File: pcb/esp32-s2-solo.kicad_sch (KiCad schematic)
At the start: 4 parts, among them U1 ESP32-S2-SOLO

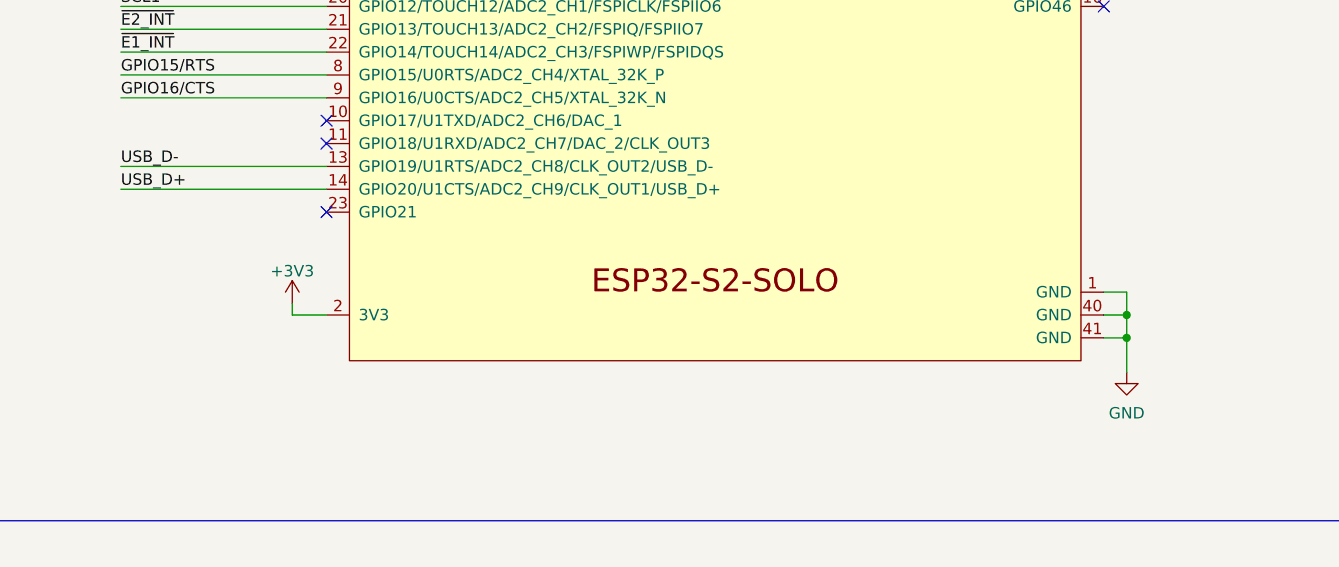
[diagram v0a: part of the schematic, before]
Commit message: fix ERC issues
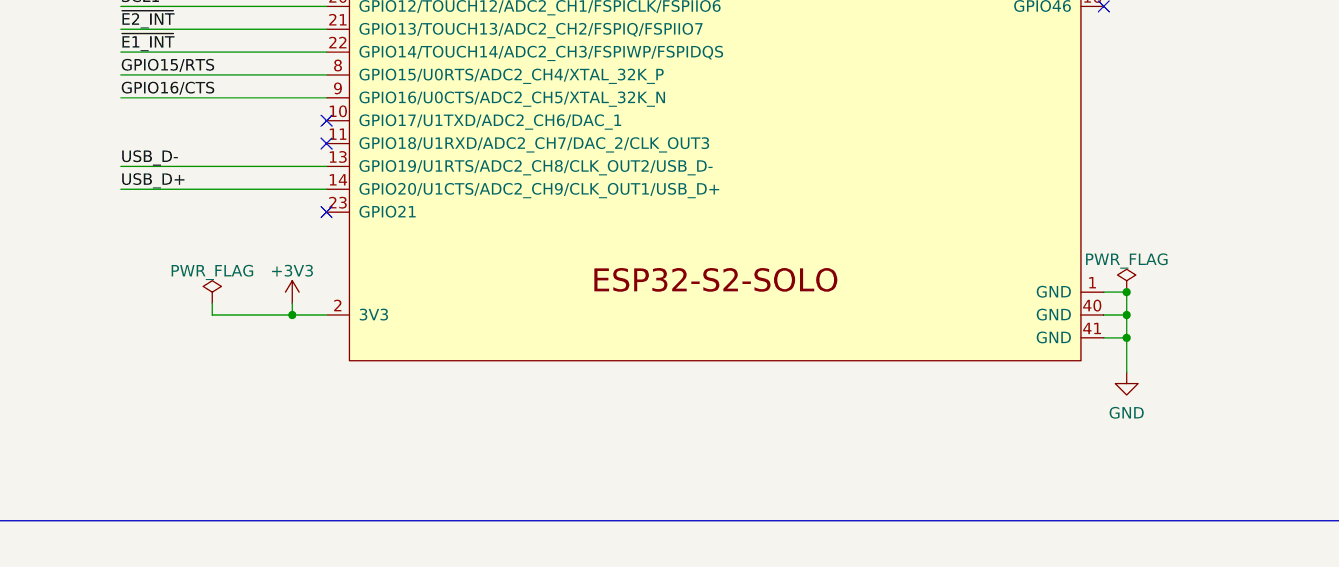
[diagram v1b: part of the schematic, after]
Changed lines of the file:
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@@
   (junction (at 250.19 115.57) (diameter 0) (color 0 0 0 0)
   )
+  (junction (at 157.48 115.57) (diameter 0) (color 0 0 0 0)
+  )
   (junction (at 68.58 172.72) (diameter 0) (color 0 0 0 0)
   )
@@
   )
   (junction (at 77.47 172.72) (diameter 0) (color 0 0 0 0)
+  )
+  (junction (at 250.19 113.03) (diameter 0) (color 0 0 0 0)
   )
   (no_connect (at 161.29 96.52))
@@
   (no_connect (at 247.65 57.15))
   (no_connect (at 247.65 54.61))
+  (wire (pts (xy 148.59 115.57) (xy 148.59 114.3))
+    (stroke (width 0) (type default) (color 0 0 0 0))
+  )
   (wire (pts (xy 161.29 86.36) (xy 138.43 86.36))
     (stroke (width 0) (type default) (color 0 0 0 0))
@@
   )
   (wire (pts (xy 29.21 175.26) (xy 29.21 180.34))
+    (stroke (width 0) (type default) (color 0 0 0 0))
+  )
+  (wire (pts (xy 157.48 115.57) (xy 148.59 115.57))
     (stroke (width 0) (type default) (color 0 0 0 0))
   )
@@
     )
     (property "Datasheet" "" (id 3) (at 74.93 162.56 0)
+      (effects (font (size 1.27 1.27)) hide)
+    )
+    (pin "1")
+  )
+  (symbol (lib_id "power:PWR_FLAG") (at 148.59 114.3 0) (unit 1)
+    (in_bom yes) (on_board yes) (fields_autoplaced)
+    (property "Reference" "#FLG0101" (id 0) (at 148.59 112.395 0)
+      (effects (font (size 1.27 1.27)) hide)
+    )
+    (property "Value" "PWR_FLAG" (id 1) (at 148.59 110.6955 0))
+    (property "Footprint" "" (id 2) (at 148.59 114.3 0)
+      (effects (font (size 1.27 1.27)) hide)
+    )
+    (property "Datasheet" "~" (id 3) (at 148.59 114.3 0)
       (effects (font (size 1.27 1.27)) hide)
     )
@@
       (effects (font (size 1.27 1.27)) hide)
     )
+    (pin "1")
+  )
+  (symbol (lib_id "power:PWR_FLAG") (at 250.19 113.03 0) (unit 1)
+    (in_bom yes) (on_board yes) (fields_autoplaced)
+    (property "Reference" "#FLG0102" (id 0) (at 250.19 111.125 0)
+      (effects (font (size 1.27 1.27)) hide)
+    )
+    (property "Value" "PWR_FLAG" (id 1) (at 250.19 109.4255 0))
+    (property "Footprint" "" (id 2) (at 250.19 113.03 0)
+      (effects (font (size 1.27 1.27)) hide)
+    )
+    (property "Datasheet" "~" (id 3) (at 250.19 113.03 0)
+      (effects (font (size 1.27 1.27)) hide)
+    )

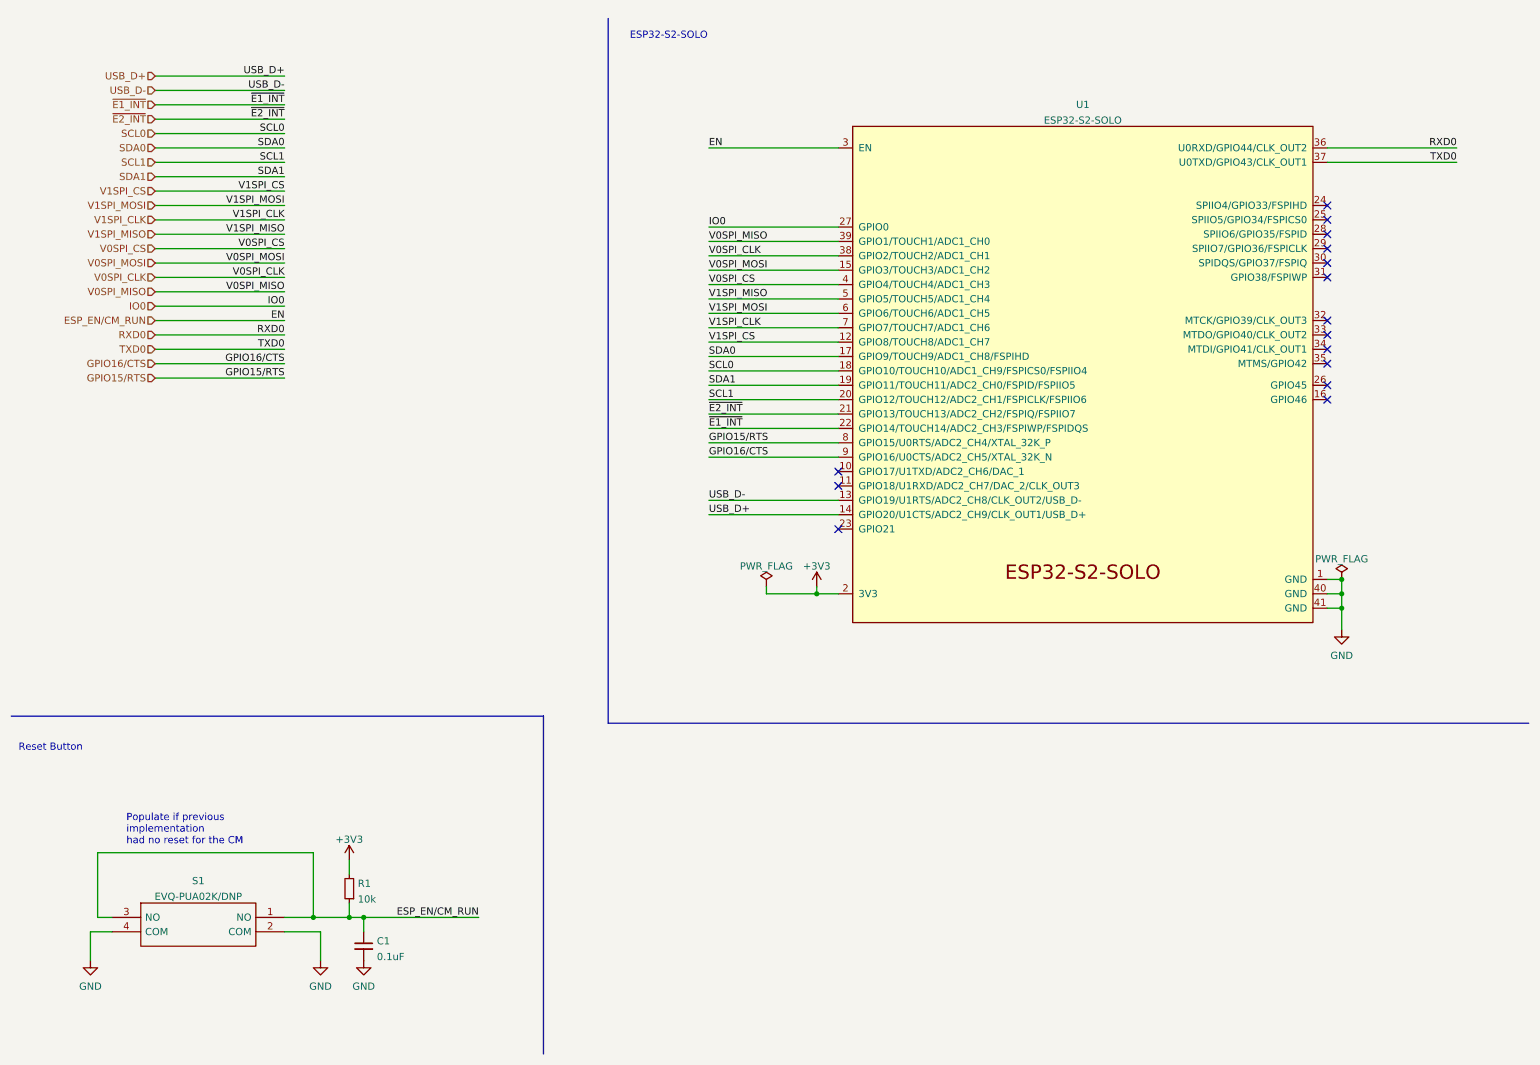
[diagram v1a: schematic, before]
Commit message: Refactored PCB Layer to have one dedicated GND Layer + rerouted traces + removed debug connector and added IO0 to the SO-DIMM connector + added decoupling caps and delay circuit for ESP32 module
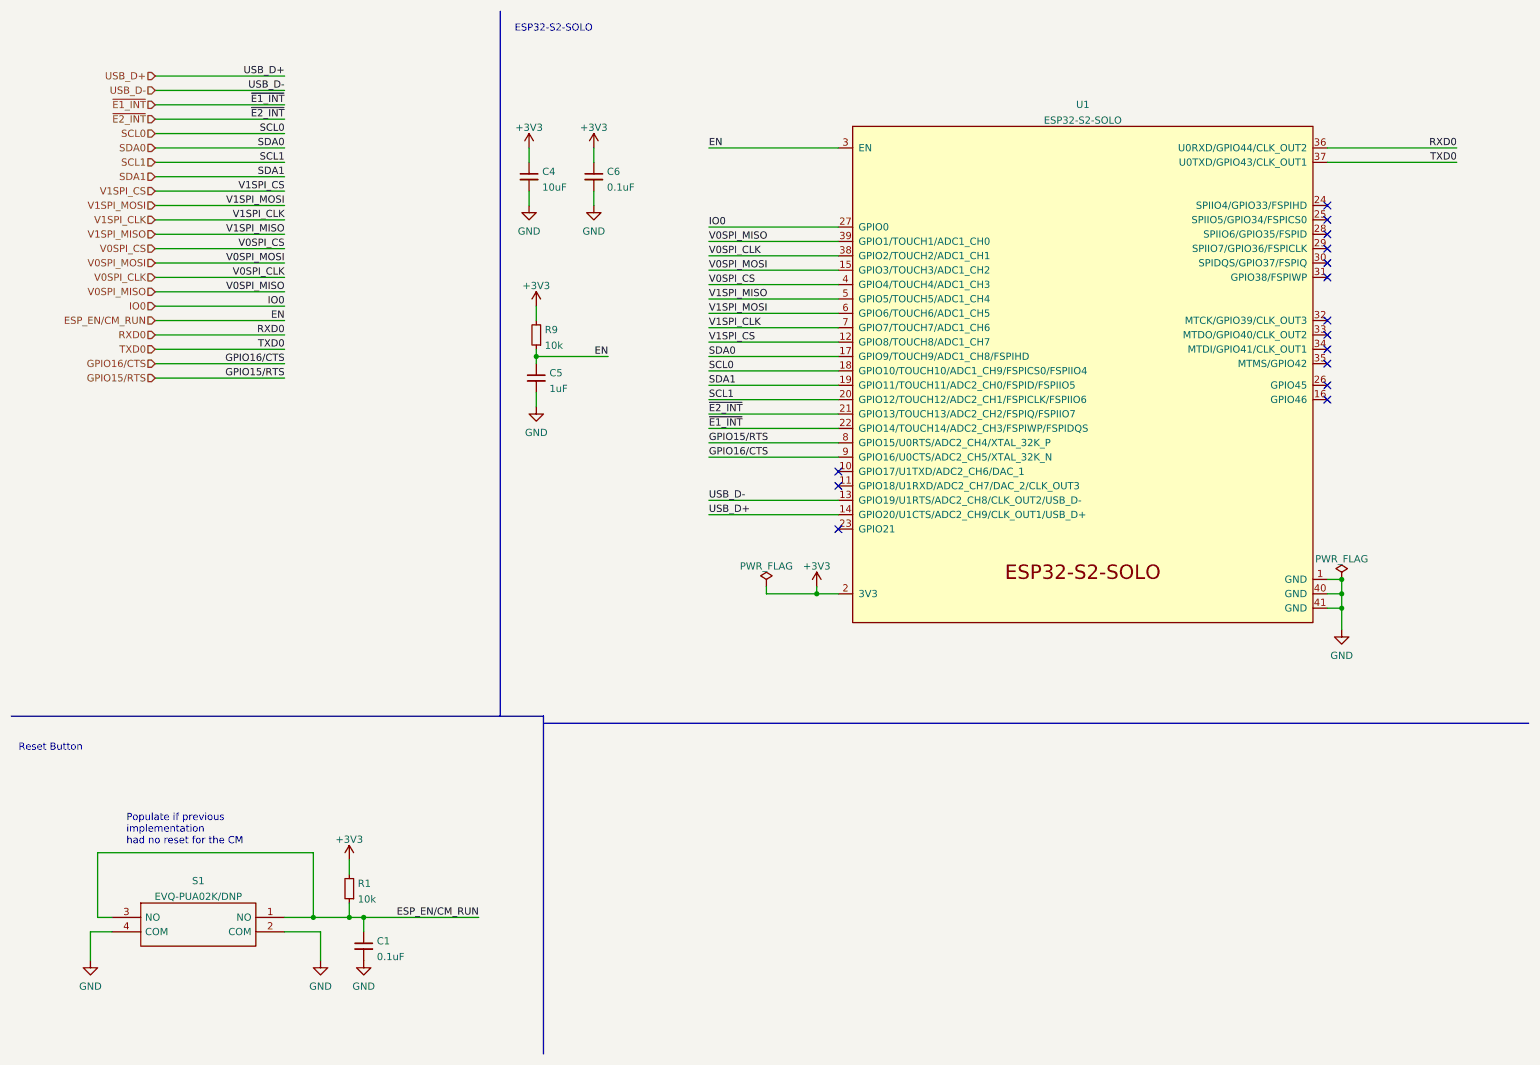
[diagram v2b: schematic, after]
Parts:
- added C4: 10uF, Capacitor_SMD:C_0603_1608Metric, symbol Device:C_Small
- added C5: 1uF, Capacitor_SMD:C_0603_1608Metric, symbol Device:C_Small
- added C6: 0.1uF, Capacitor_SMD:C_0603_1608Metric, symbol Device:C_Small
- added R9: 10k, Resistor_SMD:R_0603_1608Metric, symbol Device:R_Small
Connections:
- net +3V3: now also C4.1, C6.1, R9.2
- net ESP_EN/CM_RUN: now also C5.1, R9.1
- net GND: now also C4.2, C5.2, C6.2
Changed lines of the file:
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@@
   (junction (at 250.19 113.03) (diameter 0) (color 0 0 0 0)
+  )
+  (junction (at 107.95 73.66) (diameter 0) (color 0 0 0 0)
   )
   (no_connect (at 161.29 96.52))
@@
     (stroke (width 0) (type default) (color 0 0 0 0))
   )
-  (polyline (pts (xy 120.65 13.97) (xy 120.65 138.43))
+  (polyline (pts (xy 101.6 12.7) (xy 101.6 137.16))
     (stroke (width 0) (type default) (color 0 0 0 0))
   )
@@
     (stroke (width 0) (type default) (color 0 0 0 0))
   )
+  (wire (pts (xy 106.68 36.83) (xy 106.68 39.37))
+    (stroke (width 0) (type default) (color 0 0 0 0))
+  )
   (wire (pts (xy 161.29 115.57) (xy 157.48 115.57))
     (stroke (width 0) (type default) (color 0 0 0 0))
@@
     (stroke (width 0) (type default) (color 0 0 0 0))
   )
+  (wire (pts (xy 107.95 72.39) (xy 107.95 73.66))
+    (stroke (width 0) (type default) (color 0 0 0 0))
+  )
+  (wire (pts (xy 107.95 64.77) (xy 107.95 67.31))
+    (stroke (width 0) (type default) (color 0 0 0 0))
+  )
   (wire (pts (xy 40.64 54.61) (xy 63.5 54.61))
     (stroke (width 0) (type default) (color 0 0 0 0))
   )
-  (polyline (pts (xy 283.21 138.43) (xy 120.65 138.43))
+  (polyline (pts (xy 283.21 138.43) (xy 109.22 138.43))
+    (stroke (width 0) (type default) (color 0 0 0 0))
+  )
+  (wire (pts (xy 107.95 73.66) (xy 120.65 73.66))
+    (stroke (width 0) (type default) (color 0 0 0 0))
+  )
+  (wire (pts (xy 107.95 80.01) (xy 107.95 82.55))
     (stroke (width 0) (type default) (color 0 0 0 0))
   )
@@
     (stroke (width 0) (type default) (color 0 0 0 0))
   )
+  (wire (pts (xy 107.95 73.66) (xy 107.95 74.93))
+    (stroke (width 0) (type default) (color 0 0 0 0))
+  )
+  (wire (pts (xy 118.11 44.45) (xy 118.11 46.99))
+    (stroke (width 0) (type default) (color 0 0 0 0))
+  )
   (wire (pts (xy 157.48 115.57) (xy 157.48 114.3))
     (stroke (width 0) (type default) (color 0 0 0 0))
@@
     (stroke (width 0) (type default) (color 0 0 0 0))
   )
+  (wire (pts (xy 118.11 36.83) (xy 118.11 39.37))
+    (stroke (width 0) (type default) (color 0 0 0 0))
+  )
   (wire (pts (xy 29.21 175.26) (xy 29.21 180.34))
     (stroke (width 0) (type default) (color 0 0 0 0))
@@
     (stroke (width 0) (type default) (color 0 0 0 0))
   )
+  (wire (pts (xy 106.68 44.45) (xy 106.68 46.99))
+    (stroke (width 0) (type default) (color 0 0 0 0))
+  )
   (wire (pts (xy 138.43 36.83) (xy 161.29 36.83))
     (stroke (width 0) (type default) (color 0 0 0 0))
@@
     (stroke (width 0) (type default) (color 0 0 0 0))
   )
-  (text "ESP32-S2-SOLO" (at 124.46 17.78 0)
+  (text "ESP32-S2-SOLO" (at 104.14 16.51 0)
     (effects (font (size 1.27 1.27)) (justify left bottom))
   )
@@
     (effects (font (size 1.27 1.27)) (justify right bottom))
   )
+  (label "EN" (at 120.65 73.66 180)
+    (effects (font (size 1.27 1.27)) (justify right bottom))
+  )
   (label "SCL0" (at 138.43 76.2 0)
     (effects (font (size 1.27 1.27)) (justify left bottom))
@@
   (hierarchical_label "SCL1" (shape input) (at 40.64 39.37 180)
     (effects (font (size 1.27 1.27)) (justify right))
+  )
+  (symbol (lib_id "Device:C_Small") (at 107.95 77.47 0) (unit 1)
+    (in_bom yes) (on_board yes) (fields_autoplaced)
+    (property "Reference" "C5" (id 0) (at 110.2741 76.5678 0)
+      (effects (font (size 1.27 1.27)) (justify left))
+    )
+    (property "Value" "1uF" (id 1) (at 110.2741 79.3429 0)
+      (effects (font (size 1.27 1.27)) (justify left))
+    )
+    (property "Footprint" "Capacitor_SMD:C_0603_1608Metric" (id 2) (at 107.95 77.47 0)
+      (effects (font (size 1.27 1.27)) hide)
+    )
+    (property "Datasheet" "~" (id 3) (at 107.95 77.47 0)
+      (effects (font (size 1.27 1.27)) hide)
+    )
+    (pin "1")
+    (pin "2")
   )
   (symbol (lib_id "power:GND") (at 250.19 121.92 0) (unit 1)
@@
     )
     (property "Datasheet" "" (id 3) (at 250.19 121.92 0)
+      (effects (font (size 1.27 1.27)) hide)
+    )
+    (pin "1")
+  )
+  (symbol (lib_id "power:GND") (at 106.68 46.99 0) (unit 1)
+    (in_bom yes) (on_board yes) (fields_autoplaced)
+    (property "Reference" "#PWR0137" (id 0) (at 106.68 53.34 0)
+      (effects (font (size 1.27 1.27)) hide)
+    )
+    (property "Value" "GND" (id 1) (at 106.68 51.5525 0))
+    (property "Footprint" "" (id 2) (at 106.68 46.99 0)
+      (effects (font (size 1.27 1.27)) hide)
+    )
+    (property "Datasheet" "" (id 3) (at 106.68 46.99 0)
       (effects (font (size 1.27 1.27)) hide)
     )
@@
     (pin "1")
   )
+  (symbol (lib_id "Device:C_Small") (at 106.68 41.91 0) (unit 1)
+    (in_bom yes) (on_board yes) (fields_autoplaced)
+    (property "Reference" "C4" (id 0) (at 109.0041 41.0078 0)
+      (effects (font (size 1.27 1.27)) (justify left))
+    )
+    (property "Value" "10uF" (id 1) (at 109.0041 43.7829 0)
+      (effects (font (size 1.27 1.27)) (justify left))
+    )
+    (property "Footprint" "Capacitor_SMD:C_0603_1608Metric" (id 2) (at 106.68 41.91 0)
+      (effects (font (size 1.27 1.27)) hide)
+    )
+    (property "Datasheet" "~" (id 3) (at 106.68 41.91 0)
+      (effects (font (size 1.27 1.27)) hide)
+    )
+    (pin "1")
+    (pin "2")
+  )
+  (symbol (lib_id "power:+3V3") (at 106.68 36.83 0) (unit 1)
+    (in_bom yes) (on_board yes) (fields_autoplaced)
+    (property "Reference" "#PWR0136" (id 0) (at 106.68 40.64 0)
+      (effects (font (size 1.27 1.27)) hide)
+    )
+    (property "Value" "+3V3" (id 1) (at 106.68 33.2255 0))
+    (property "Footprint" "" (id 2) (at 106.68 36.83 0)
+      (effects (font (size 1.27 1.27)) hide)
+    )
+    (property "Datasheet" "" (id 3) (at 106.68 36.83 0)
+      (effects (font (size 1.27 1.27)) hide)
+    )
+    (pin "1")
+  )
   (symbol (lib_id "power:GND") (at 29.21 180.34 0) (unit 1)
     (in_bom yes) (on_board yes) (fields_autoplaced)
@@
     (pin "1")
   )
+  (symbol (lib_id "power:GND") (at 118.11 46.99 0) (unit 1)
+    (in_bom yes) (on_board yes) (fields_autoplaced)
+    (property "Reference" "#PWR0135" (id 0) (at 118.11 53.34 0)
+      (effects (font (size 1.27 1.27)) hide)
+    )
+    (property "Value" "GND" (id 1) (at 118.11 51.5525 0))
+    (property "Footprint" "" (id 2) (at 118.11 46.99 0)
+      (effects (font (size 1.27 1.27)) hide)
+    )
+    (property "Datasheet" "" (id 3) (at 118.11 46.99 0)
+      (effects (font (size 1.27 1.27)) hide)
+    )
+    (pin "1")
+  )
+  (symbol (lib_id "Device:R_Small") (at 107.95 69.85 180) (unit 1)
+    (in_bom yes) (on_board yes) (fields_autoplaced)
+    (property "Reference" "R9" (id 0) (at 109.4486 68.9415 0)
+      (effects (font (size 1.27 1.27)) (justify right))
+    )
+    (property "Value" "10k" (id 1) (at 109.4486 71.7166 0)
+      (effects (font (size 1.27 1.27)) (justify right))
+    )
+    (property "Footprint" "Resistor_SMD:R_0603_1608Metric" (id 2) (at 107.95 69.85 0)
+      (effects (font (size 1.27 1.27)) hide)
+    )
+    (property "Datasheet" "~" (id 3) (at 107.95 69.85 0)
+      (effects (font (size 1.27 1.27)) hide)
+    )
+    (pin "1")
+    (pin "2")
+  )
   (symbol (lib_id "Device:C_Small") (at 77.47 177.8 0) (unit 1)
     (in_bom yes) (on_board yes) (fields_autoplaced)
@@
     (pin "2")
   )
+  (symbol (lib_id "Device:C_Small") (at 118.11 41.91 0) (unit 1)
+    (in_bom yes) (on_board yes) (fields_autoplaced)
+    (property "Reference" "C6" (id 0) (at 120.4341 41.0078 0)
+      (effects (font (size 1.27 1.27)) (justify left))
+    )
+    (property "Value" "0.1uF" (id 1) (at 120.4341 43.7829 0)
+      (effects (font (size 1.27 1.27)) (justify left))
+    )
+    (property "Footprint" "Capacitor_SMD:C_0603_1608Metric" (id 2) (at 118.11 41.91 0)
+      (effects (font (size 1.27 1.27)) hide)
+    )
+    (property "Datasheet" "~" (id 3) (at 118.11 41.91 0)
+      (effects (font (size 1.27 1.27)) hide)
+    )
+    (pin "1")
+    (pin "2")
+  )
+  (symbol (lib_id "power:+3V3") (at 118.11 36.83 0) (unit 1)
+    (in_bom yes) (on_board yes) (fields_autoplaced)
+    (property "Reference" "#PWR0138" (id 0) (at 118.11 40.64 0)
+      (effects (font (size 1.27 1.27)) hide)
+    )
+    (property "Value" "+3V3" (id 1) (at 118.11 33.2255 0))
+    (property "Footprint" "" (id 2) (at 118.11 36.83 0)
+      (effects (font (size 1.27 1.27)) hide)
+    )
+    (property "Datasheet" "" (id 3) (at 118.11 36.83 0)
+      (effects (font (size 1.27 1.27)) hide)
+    )
+    (pin "1")
+  )
   (symbol (lib_id "power:+3V3") (at 157.48 114.3 0) (unit 1)
     (in_bom yes) (on_board yes) (fields_autoplaced)
@@
     )
     (property "Datasheet" "" (id 3) (at 157.48 114.3 0)
+      (effects (font (size 1.27 1.27)) hide)
+    )
+    (pin "1")
+  )
+  (symbol (lib_id "power:+3V3") (at 107.95 64.77 0) (unit 1)
+    (in_bom yes) (on_board yes) (fields_autoplaced)
+    (property "Reference" "#PWR0133" (id 0) (at 107.95 68.58 0)
+      (effects (font (size 1.27 1.27)) hide)
+    )
+    (property "Value" "+3V3" (id 1) (at 107.95 61.1655 0))
+    (property "Footprint" "" (id 2) (at 107.95 64.77 0)
+      (effects (font (size 1.27 1.27)) hide)
+    )
+    (property "Datasheet" "" (id 3) (at 107.95 64.77 0)
       (effects (font (size 1.27 1.27)) hide)
     )
@@
     (pin "4")
   )
+  (symbol (lib_id "power:GND") (at 107.95 82.55 0) (unit 1)
+    (in_bom yes) (on_board yes) (fields_autoplaced)
+    (property "Reference" "#PWR0134" (id 0) (at 107.95 88.9 0)
+      (effects (font (size 1.27 1.27)) hide)
+    )
+    (property "Value" "GND" (id 1) (at 107.95 87.1125 0))
+    (property "Footprint" "" (id 2) (at 107.95 82.55 0)
+      (effects (font (size 1.27 1.27)) hide)
+    )
+    (property "Datasheet" "" (id 3) (at 107.95 82.55 0)
+      (effects (font (size 1.27 1.27)) hide)
+    )
+    (pin "1")
+  )
 )
